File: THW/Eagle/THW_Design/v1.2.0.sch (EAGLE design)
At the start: 23 parts

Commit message: More work
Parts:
- R_CURRENT: value (none) -> 100
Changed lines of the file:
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@@
 <?xml version="1.0" encoding="utf-8"?>
 <!DOCTYPE eagle SYSTEM "eagle.dtd">
-<eagle version="9.1.3">
+<eagle version="9.2.2">
 <drawing>
 <settings>
@@
 </classes>
 <parts>
-<part name="R_CURRENT" library="resistor" library_urn="urn:adsk.eagle:library:348" deviceset="R-US_" device="M0805" package3d_urn="urn:adsk.eagle:package:26079/1"/>
+<part name="R_CURRENT" library="resistor" library_urn="urn:adsk.eagle:library:348" deviceset="R-US_" device="M0805" package3d_urn="urn:adsk.eagle:package:26079/1" value="100"/>
 <part name="LONG_HW+" library="WIREPOINT" deviceset="WIREPOINT_1" device="A"/>
 <part name="LONG_HW-" library="WIREPOINT" deviceset="WIREPOINT_1" device="A"/>
@@
 </plain>
 <instances>
-<instance part="R_CURRENT" gate="G$1" x="160.02" y="195.58">
+<instance part="R_CURRENT" gate="G$1" x="160.02" y="195.58" smashed="yes">
 <attribute name="NAME" x="156.21" y="197.0786" size="1.778" layer="95"/>
 <attribute name="VALUE" x="156.21" y="192.278" size="1.778" layer="96"/>
 </instance>
-<instance part="LONG_HW+" gate="G$1" x="180.34" y="55.88" rot="R180">
+<instance part="LONG_HW+" gate="G$1" x="180.34" y="55.88" smashed="yes" rot="R180">
 <attribute name="NAME" x="180.34" y="58.42" size="1.27" layer="95" rot="R180"/>
 </instance>
-<instance part="LONG_HW-" gate="G$1" x="180.34" y="35.56">
+<instance part="LONG_HW-" gate="G$1" x="180.34" y="35.56" smashed="yes">
 <attribute name="NAME" x="180.34" y="33.02" size="1.27" layer="95"/>
 </instance>
-<instance part="SHORT_HW-" gate="G$1" x="180.34" y="119.38">
+<instance part="SHORT_HW-" gate="G$1" x="180.34" y="119.38" smashed="yes">
 <attribute name="NAME" x="180.34" y="116.84" size="1.27" layer="95"/>
 </instance>
-<instance part="SHORT_HW+" gate="G$1" x="180.34" y="134.62" rot="R180">
+<instance part="SHORT_HW+" gate="G$1" x="180.34" y="134.62" smashed="yes" rot="R180">
 <attribute name="NAME" x="180.34" y="137.16" size="1.27" layer="95" rot="R180"/>
 </instance>
-<instance part="WB_SENS2" gate="G$1" x="218.44" y="218.44">
+<instance part="WB_SENS2" gate="G$1" x="218.44" y="218.44" smashed="yes">
 <attribute name="NAME" x="218.44" y="248.92" size="1.778" layer="95"/>
 </instance>
-<instance part="WB_SENS1" gate="G$1" x="231.14" y="86.36" rot="R180">
+<instance part="WB_SENS1" gate="G$1" x="231.14" y="86.36" smashed="yes" rot="R180">
 <attribute name="NAME" x="231.14" y="55.88" size="1.778" layer="95" rot="R180"/>
 </instance>
-<instance part="POWER" gate="G$1" x="48.26" y="198.12">
+<instance part="POWER" gate="G$1" x="48.26" y="198.12" smashed="yes">
 <attribute name="NAME" x="48.26" y="228.6" size="1.778" layer="95"/>
 </instance>
-<instance part="PT_SENS1" gate="G$1" x="281.94" y="325.12">
+<instance part="PT_SENS1" gate="G$1" x="281.94" y="325.12" smashed="yes">
 <attribute name="NAME" x="281.94" y="355.6" size="1.778" layer="95"/>
 </instance>
-<instance part="PT_SENS2" gate="G$1" x="154.94" y="322.58">
+<instance part="PT_SENS2" gate="G$1" x="154.94" y="322.58" smashed="yes">
 <attribute name="NAME" x="154.94" y="353.06" size="1.778" layer="95"/>
 </instance>
-<instance part="PT$1" gate="G$1" x="86.36" y="289.56">
+<instance part="PT$1" gate="G$1" x="86.36" y="289.56" smashed="yes">
 <attribute name="NAME" x="86.614" y="292.862" size="1.778" layer="95"/>
 <attribute name="VALUE" x="86.36" y="284.48" size="1.778" layer="96"/>
 </instance>
-<instance part="PT$2" gate="G$1" x="124.46" y="289.56">
+<instance part="PT$2" gate="G$1" x="124.46" y="289.56" smashed="yes">
 <attribute name="NAME" x="124.714" y="292.862" size="1.778" layer="95"/>
 <attribute name="VALUE" x="124.46" y="284.48" size="1.778" layer="96"/>
 </instance>
-<instance part="PT$3" gate="G$1" x="170.18" y="289.56">
+<instance part="PT$3" gate="G$1" x="170.18" y="289.56" smashed="yes">
 <attribute name="NAME" x="170.434" y="292.862" size="1.778" layer="95"/>
 <attribute name="VALUE" x="170.18" y="284.48" size="1.778" layer="96"/>
 </instance>
-<instance part="PT$4" gate="G$1" x="215.9" y="289.56">
+<instance part="PT$4" gate="G$1" x="215.9" y="289.56" smashed="yes">
 <attribute name="NAME" x="216.154" y="292.862" size="1.778" layer="95"/>
 <attribute name="VALUE" x="215.9" y="284.48" size="1.778" layer="96"/>
 </instance>
-<instance part="PT$5" gate="G$1" x="264.16" y="289.56">
+<instance part="PT$5" gate="G$1" x="264.16" y="289.56" smashed="yes">
 <attribute name="NAME" x="264.414" y="292.862" size="1.778" layer="95"/>
 <attribute name="VALUE" x="264.16" y="284.48" size="1.778" layer="96"/>
 </instance>
-<instance part="PT$6" gate="G$1" x="309.88" y="289.56">
+<instance part="PT$6" gate="G$1" x="309.88" y="289.56" smashed="yes">
 <attribute name="NAME" x="310.134" y="292.862" size="1.778" layer="95"/>
 <attribute name="VALUE" x="309.88" y="284.48" size="1.778" layer="96"/>
 </instance>
-<instance part="POT_1" gate="G$1" x="177.8" y="165.1" rot="R90">
+<instance part="POT_1" gate="G$1" x="177.8" y="165.1" smashed="yes" rot="R90">
 <attribute name="NAME" x="175.26" y="165.1" size="1.778" layer="95" rot="R90"/>
 </instance>
-<instance part="POT_2" gate="G$1" x="177.8" y="0" rot="R90">
+<instance part="POT_2" gate="G$1" x="177.8" y="0" smashed="yes" rot="R90">
 <attribute name="NAME" x="175.26" y="0" size="1.778" layer="95" rot="R90"/>
 </instance>
-<instance part="POT_3" gate="G$1" x="271.78" y="144.78" rot="R90">
+<instance part="POT_3" gate="G$1" x="271.78" y="144.78" smashed="yes" rot="R90">
 <attribute name="NAME" x="269.24" y="144.78" size="1.778" layer="95" rot="R90"/>
 </instance>
-<instance part="POT_4" gate="G$1" x="271.78" y="30.48" rot="R90">
+<instance part="POT_4" gate="G$1" x="271.78" y="30.48" smashed="yes" rot="R90">
 <attribute name="NAME" x="269.24" y="30.48" size="1.778" layer="95" rot="R90"/>
 </instance>
-<instance part="PAD1" gate="1" x="109.22" y="-43.18">
+<instance part="PAD1" gate="1" x="109.22" y="-43.18" smashed="yes">
 <attribute name="NAME" x="108.077" y="-41.3258" size="1.778" layer="95"/>
 <attribute name="VALUE" x="108.077" y="-46.482" size="1.778" layer="96"/>
 </instance>
-<instance part="PAD2" gate="1" x="109.22" y="-50.8">
+<instance part="PAD2" gate="1" x="109.22" y="-50.8" smashed="yes">
 <attribute name="NAME" x="108.077" y="-48.9458" size="1.778" layer="95"/>
 <attribute name="VALUE" x="108.077" y="-54.102" size="1.778" layer="96"/>
 </instance>
-<instance part="PAD3" gate="1" x="109.22" y="-58.42">
+<instance part="PAD3" gate="1" x="109.22" y="-58.42" smashed="yes">
 <attribute name="NAME" x="108.077" y="-56.5658" size="1.778" layer="95"/>
 <attribute name="VALUE" x="108.077" y="-61.722" size="1.778" layer="96"/>
 </instance>
-<instance part="SUPPLY1" gate="GND" x="76.2" y="226.06" rot="R90">
+<instance part="SUPPLY1" gate="GND" x="76.2" y="226.06" smashed="yes" rot="R90">
 <attribute name="VALUE" x="79.375" y="224.155" size="1.778" layer="96" rot="R90"/>
 </instance>
-<instance part="SUPPLY2" gate="GND" x="71.12" y="223.52" rot="R90">
+<instance part="SUPPLY2" gate="GND" x="71.12" y="223.52" smashed="yes" rot="R90">
 <attribute name="VALUE" x="74.295" y="221.615" size="1.778" layer="96" rot="R90"/>
 </instance>
-<instance part="SUPPLY3" gate="GND" x="246.38" y="246.38" rot="R90">
+<instance part="SUPPLY3" gate="GND" x="246.38" y="246.38" smashed="yes" rot="R90">
 <attribute name="VALUE" x="249.555" y="244.475" size="1.778" layer="96" rot="R90"/>
 </instance>
-<instance part="SUPPLY4" gate="GND" x="241.3" y="243.84" rot="R90">
+<instance part="SUPPLY4" gate="GND" x="241.3" y="243.84" smashed="yes" rot="R90">
 <attribute name="VALUE" x="244.475" y="241.935" size="1.778" layer="96" rot="R90"/>
 </instance>
-<instance part="SUPPLY5" gate="GND" x="182.88" y="350.52" rot="R90">
+<instance part="SUPPLY5" gate="GND" x="182.88" y="350.52" smashed="yes" rot="R90">
 <attribute name="VALUE" x="186.055" y="348.615" size="1.778" layer="96" rot="R90"/>
 </instance>
-<instance part="SUPPLY6" gate="GND" x="180.34" y="347.98" rot="R90">
+<instance part="SUPPLY6" gate="GND" x="180.34" y="347.98" smashed="yes" rot="R90">
 <attribute name="VALUE" x="183.515" y="346.075" size="1.778" layer="96" rot="R90"/>
 </instance>
-<instance part="SUPPLY7" gate="GND" x="312.42" y="353.06" rot="R90">
+<instance part="SUPPLY7" gate="GND" x="312.42" y="353.06" smashed="yes" rot="R90">
 <attribute name="VALUE" x="315.595" y="351.155" size="1.778" layer="96" rot="R90"/>
 </instance>
-<instance part="SUPPLY8" gate="GND" x="307.34" y="350.52" rot="R90">
+<instance part="SUPPLY8" gate="GND" x="307.34" y="350.52" smashed="yes" rot="R90">
 <attribute name="VALUE" x="310.515" y="348.615" size="1.778" layer="96" rot="R90"/>
 </instance>
-<instance part="SUPPLY9" gate="GND" x="208.28" y="60.96" rot="R270">
+<instance part="SUPPLY9" gate="GND" x="208.28" y="60.96" smashed="yes" rot="R270">
 <attribute name="VALUE" x="205.105" y="62.865" size="1.778" layer="96" rot="R270"/>
 </instance>
-<instance part="SUPPLY10" gate="GND" x="203.2" y="58.42" rot="R270">
+<instance part="SUPPLY10" gate="GND" x="203.2" y="58.42" smashed="yes" rot="R270">
 <attribute name="VALUE" x="200.025" y="60.325" size="1.778" layer="96" rot="R270"/>
 </instance>
@@
 <junction x="177.8" y="-15.24"/>
 <label x="167.64" y="-12.7" size="1.778" layer="95" rot="R180" xref="yes"/>
-</segment>
-<segment>
+<junction x="177.8" y="-12.7"/>
+</segment>
+<segment>

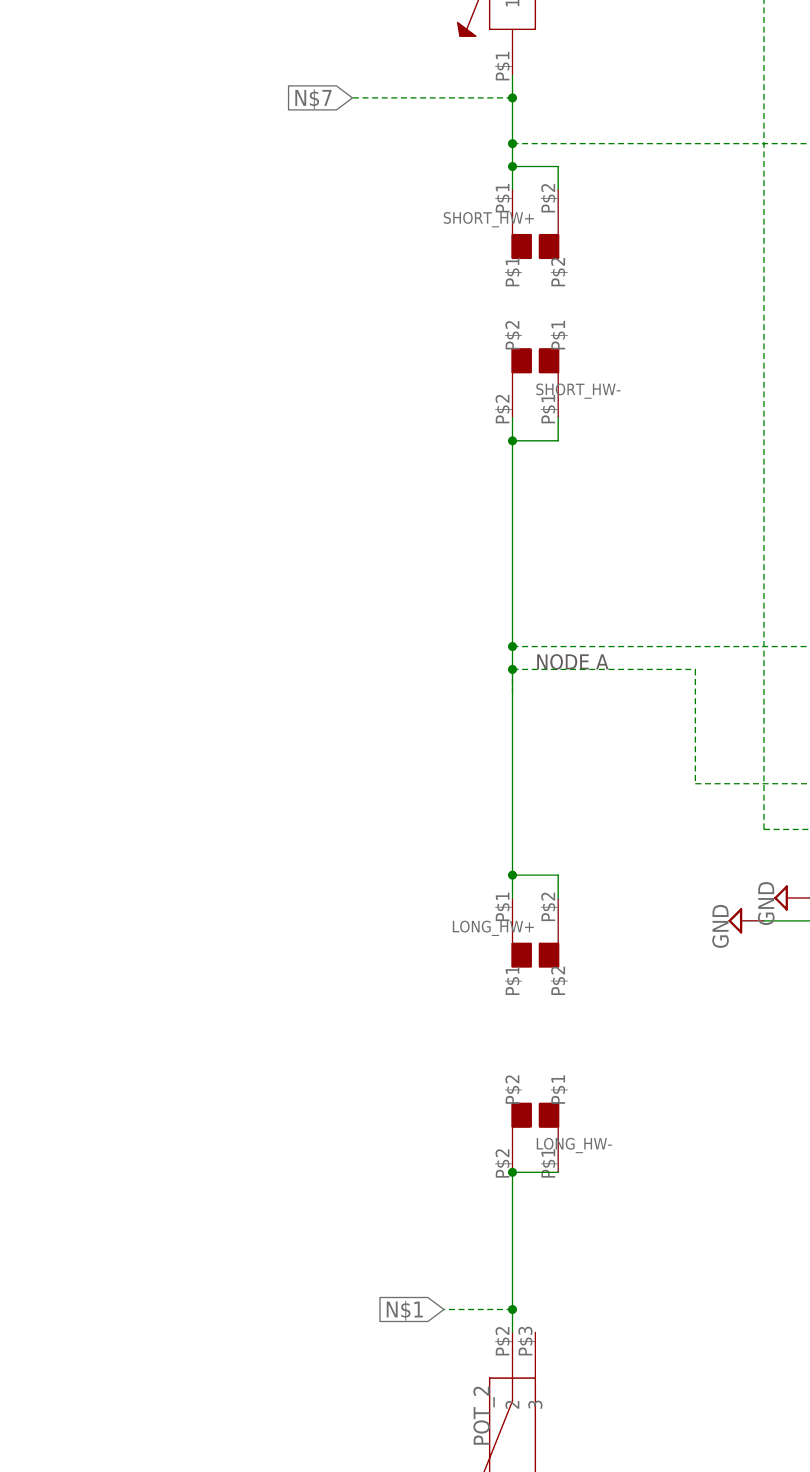
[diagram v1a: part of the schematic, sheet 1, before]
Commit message: fix sheild pin
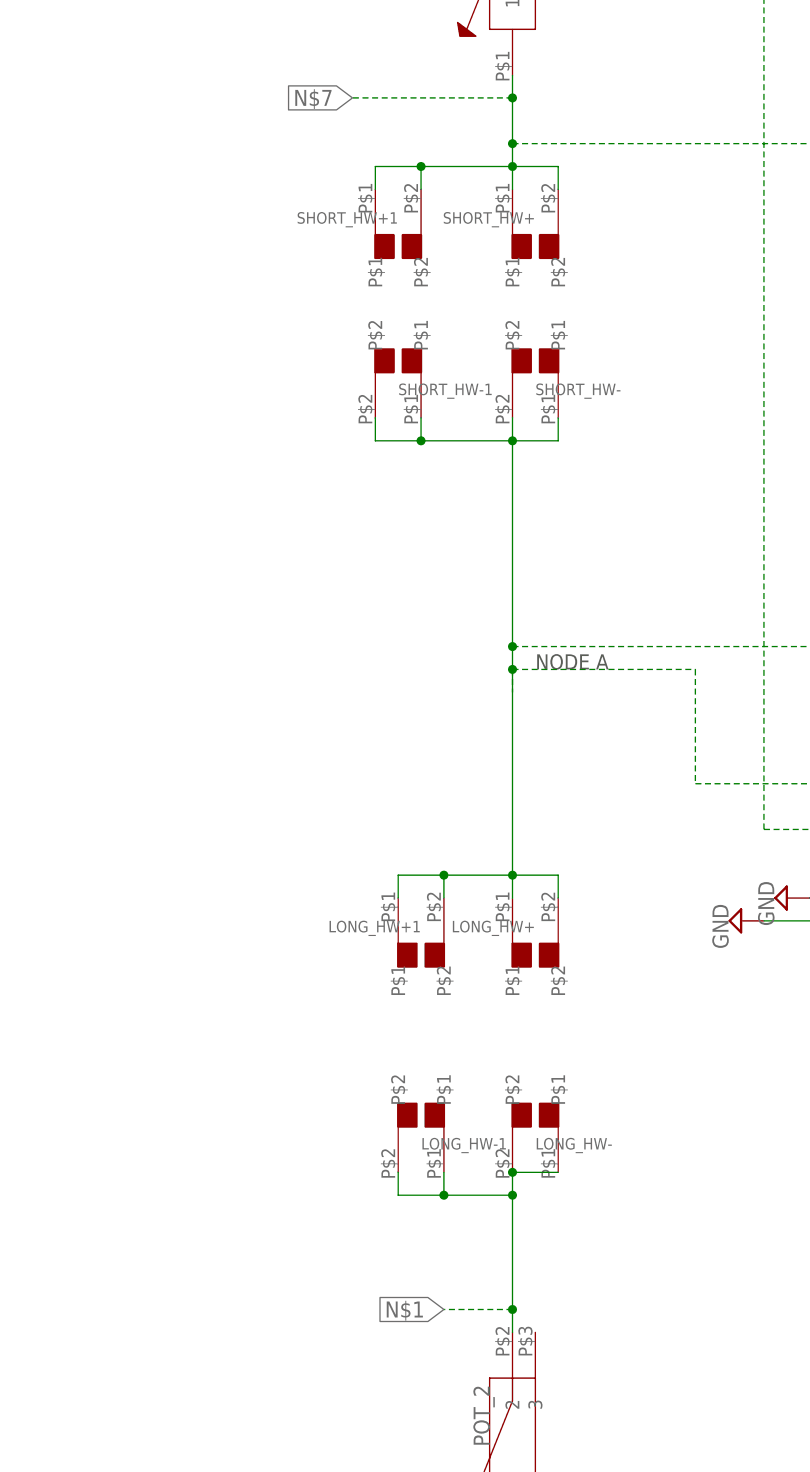
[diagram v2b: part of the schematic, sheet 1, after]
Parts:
- added LONG_HW+1, LONG_HW-1, SHORT_HW+1, SHORT_HW-1: WIREPOINT_1A, WIREPOINT:WIREPOINT_1A
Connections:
- net N$1: now also LONG_HW-1.P$1, LONG_HW-1.P$2
- net N$7: now also SHORT_HW+1.P$1, SHORT_HW+1.P$2
- net SHORT_HW-: now also LONG_HW+1.P$1, LONG_HW+1.P$2, SHORT_HW-1.P$1, SHORT_HW-1.P$2
